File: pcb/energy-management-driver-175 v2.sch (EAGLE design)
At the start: 57 parts, among them T1 BT138-V, T2 BT138-V, T3 BT138-V, T4 BT138-V, T5 BT138-V, T6 BT138-V, T7 BT138-V, T8 BT138-V

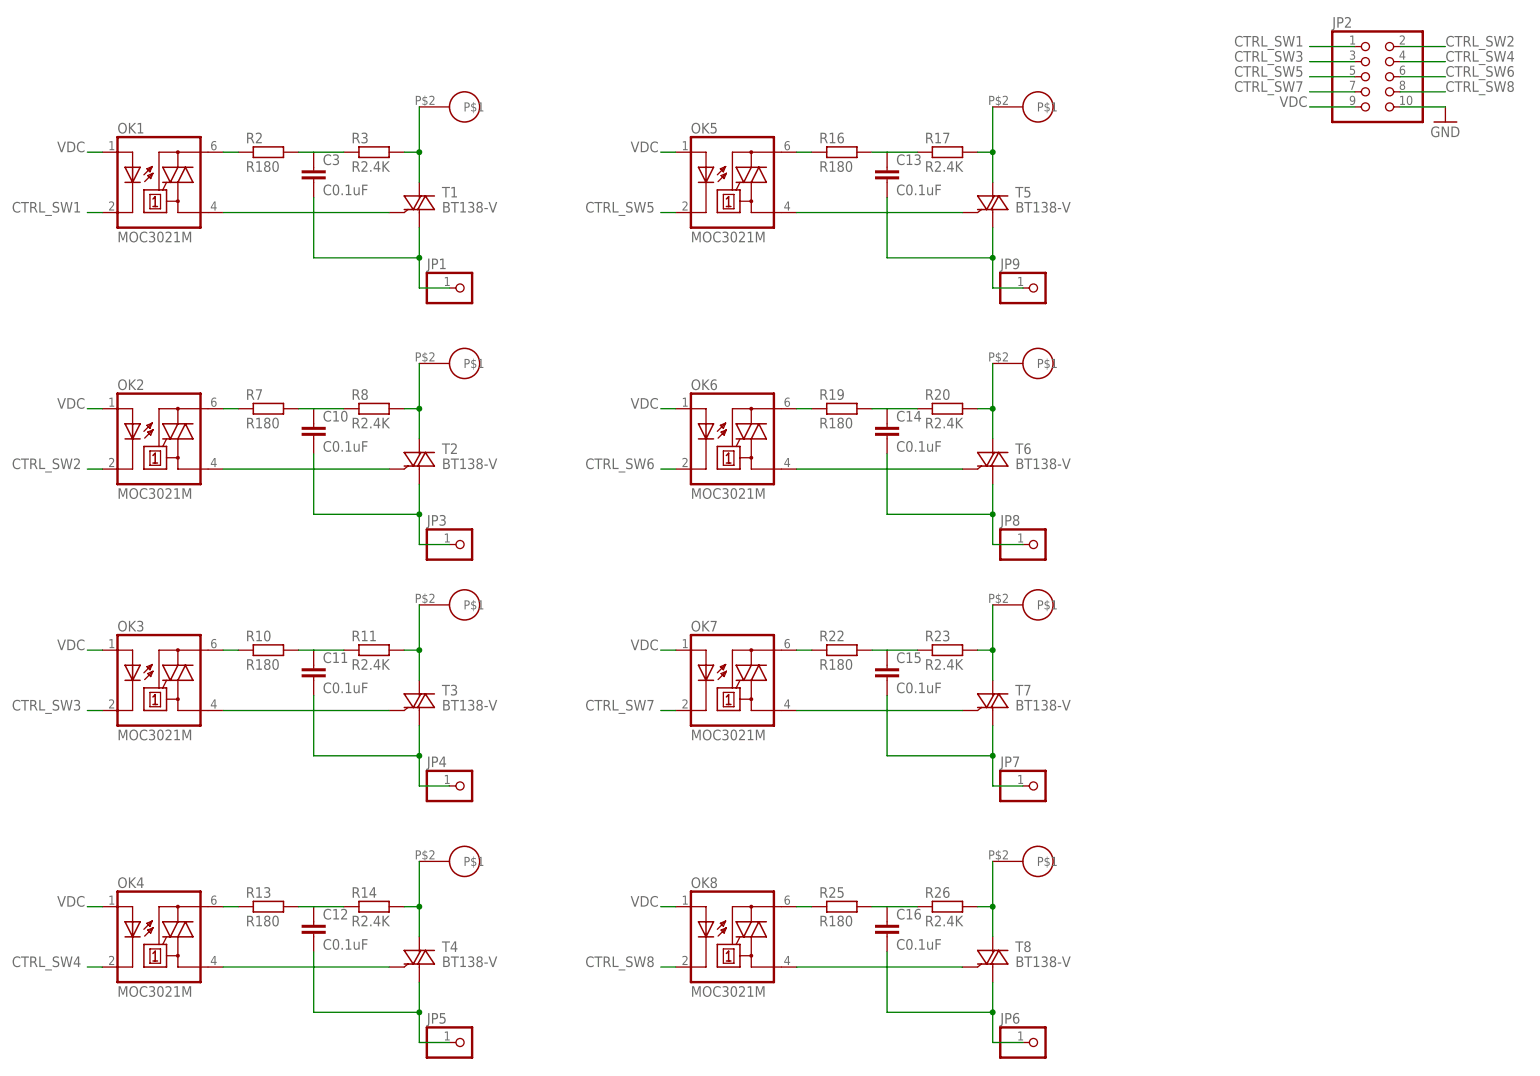
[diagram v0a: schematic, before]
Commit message: update holes in driver board
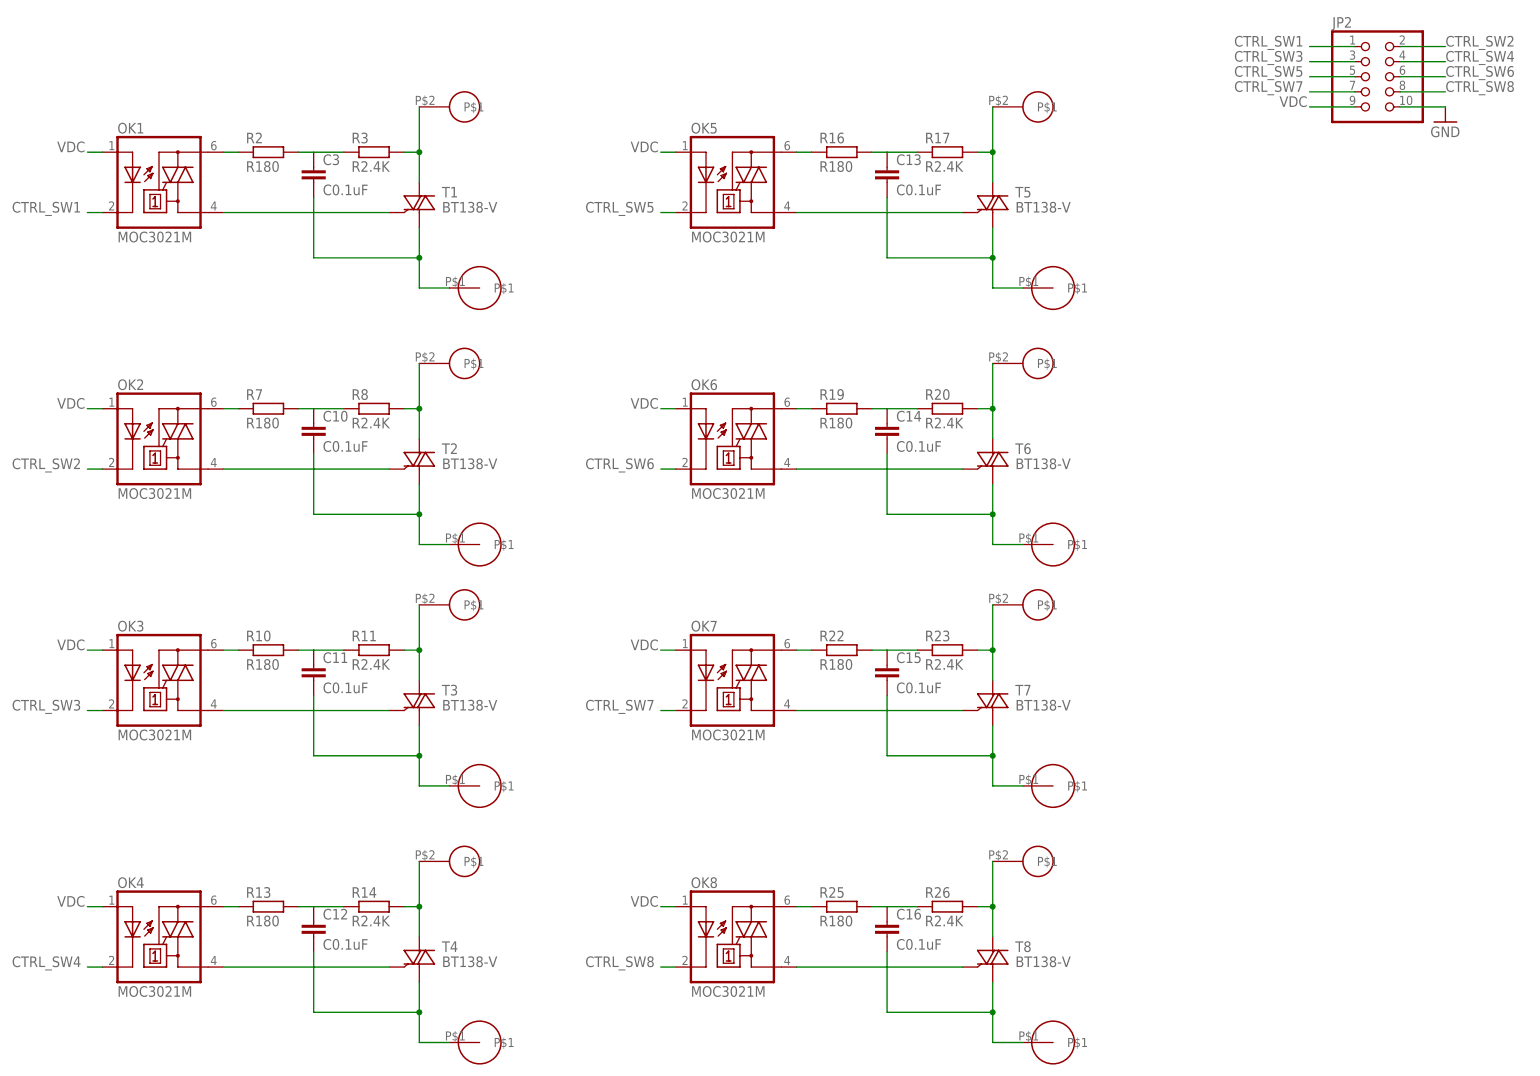
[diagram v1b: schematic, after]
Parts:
- removed JP1, JP3, JP4, JP5, JP6, JP7, JP8, JP9: (no value), pinhead:PINHD-1X1
- added U$10, U$11, U$12, U$13, U$14, U$15, U$16, U$9: CONN-CABLE, bontor:CONN-CABLE
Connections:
- net N$15: now also U$11.P$1; no longer JP3.1
- net N$21: now also U$14.P$1; no longer JP4.1
- net N$27: now also U$13.P$1; no longer JP5.1
- net N$33: now also U$10.P$1; no longer JP9.1
- net N$39: now also U$12.P$1; no longer JP8.1
- net N$45: now also U$15.P$1; no longer JP7.1
- net N$51: now also U$16.P$1; no longer JP6.1
- net N$6: now also U$9.P$1; no longer JP1.1
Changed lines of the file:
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@@
 <part name="JP2" library="pinhead" deviceset="PINHD-2X5" device=""/>
 <part name="GND2" library="SparkFun-Aesthetics" deviceset="GND" device=""/>
-<part name="JP1" library="pinhead" deviceset="PINHD-1X1" device=""/>
 <part name="U$1" library="bontor" deviceset="CONN-SKUN" device=""/>
 <part name="U$2" library="bontor" deviceset="CONN-SKUN" device=""/>
@@
 <part name="U$7" library="bontor" deviceset="CONN-SKUN" device=""/>
 <part name="U$8" library="bontor" deviceset="CONN-SKUN" device=""/>
-<part name="JP3" library="pinhead" deviceset="PINHD-1X1" device=""/>
-<part name="JP4" library="pinhead" deviceset="PINHD-1X1" device=""/>
-<part name="JP5" library="pinhead" deviceset="PINHD-1X1" device=""/>
-<part name="JP6" library="pinhead" deviceset="PINHD-1X1" device=""/>
-<part name="JP7" library="pinhead" deviceset="PINHD-1X1" device=""/>
-<part name="JP8" library="pinhead" deviceset="PINHD-1X1" device=""/>
-<part name="JP9" library="pinhead" deviceset="PINHD-1X1" device=""/>
+<part name="U$9" library="bontor" deviceset="CONN-CABLE" device=""/>
+<part name="U$10" library="bontor" deviceset="CONN-CABLE" device=""/>
+<part name="U$11" library="bontor" deviceset="CONN-CABLE" device=""/>
+<part name="U$12" library="bontor" deviceset="CONN-CABLE" device=""/>
+<part name="U$13" library="bontor" deviceset="CONN-CABLE" device=""/>
+<part name="U$14" library="bontor" deviceset="CONN-CABLE" device=""/>
+<part name="U$15" library="bontor" deviceset="CONN-CABLE" device=""/>
+<part name="U$16" library="bontor" deviceset="CONN-CABLE" device=""/>
 </parts>
 <sheets>
@@
 <instance part="JP2" gate="A" x="241.3" y="172.72"/>
 <instance part="GND2" gate="1" x="254" y="165.1"/>
-<instance part="JP1" gate="G$1" x="88.9" y="137.16"/>
 <instance part="U$1" gate="G$1" x="88.9" y="167.64"/>
 <instance part="U$2" gate="G$1" x="88.9" y="124.46"/>
@@
 <instance part="U$7" gate="G$1" x="185.42" y="124.46"/>
 <instance part="U$8" gate="G$1" x="185.42" y="167.64"/>
-<instance part="JP3" gate="G$1" x="88.9" y="93.98"/>
-<instance part="JP4" gate="G$1" x="88.9" y="53.34"/>
-<instance part="JP5" gate="G$1" x="88.9" y="10.16"/>
-<instance part="JP6" gate="G$1" x="185.42" y="10.16"/>
-<instance part="JP7" gate="G$1" x="185.42" y="53.34"/>
-<instance part="JP8" gate="G$1" x="185.42" y="93.98"/>
-<instance part="JP9" gate="G$1" x="185.42" y="137.16"/>
+<instance part="U$9" gate="G$1" x="91.44" y="137.16"/>
+<instance part="U$10" gate="G$1" x="187.96" y="137.16"/>
+<instance part="U$11" gate="G$1" x="91.44" y="93.98"/>
+<instance part="U$12" gate="G$1" x="187.96" y="93.98"/>
+<instance part="U$13" gate="G$1" x="91.44" y="10.16"/>
+<instance part="U$14" gate="G$1" x="91.44" y="53.34"/>
+<instance part="U$15" gate="G$1" x="187.96" y="53.34"/>
+<instance part="U$16" gate="G$1" x="187.96" y="10.16"/>
 </instances>
 <busses>
@@
 <wire x1="81.28" y1="137.16" x2="81.28" y2="142.24" width="0.1524" layer="91"/>
 <junction x="81.28" y="142.24"/>
-<pinref part="JP1" gate="G$1" pin="1"/>
 <wire x1="86.36" y1="137.16" x2="81.28" y2="137.16" width="0.1524" layer="91"/>
+<pinref part="U$9" gate="G$1" pin="P$1"/>
 </segment>
 </net>
@@
 <wire x1="81.28" y1="93.98" x2="81.28" y2="99.06" width="0.1524" layer="91"/>
 <junction x="81.28" y="99.06"/>
-<pinref part="JP3" gate="G$1" pin="1"/>
 <wire x1="86.36" y1="93.98" x2="81.28" y2="93.98" width="0.1524" layer="91"/>
+<pinref part="U$11" gate="G$1" pin="P$1"/>
 </segment>
 </net>
@@
 <wire x1="81.28" y1="53.34" x2="81.28" y2="58.42" width="0.1524" layer="91"/>
 <junction x="81.28" y="58.42"/>
-<pinref part="JP4" gate="G$1" pin="1"/>
 <wire x1="86.36" y1="53.34" x2="81.28" y2="53.34" width="0.1524" layer="91"/>
+<pinref part="U$14" gate="G$1" pin="P$1"/>
 </segment>
 </net>
@@
 <wire x1="81.28" y1="10.16" x2="81.28" y2="15.24" width="0.1524" layer="91"/>
 <junction x="81.28" y="15.24"/>
-<pinref part="JP5" gate="G$1" pin="1"/>
 <wire x1="86.36" y1="10.16" x2="81.28" y2="10.16" width="0.1524" layer="91"/>
+<pinref part="U$13" gate="G$1" pin="P$1"/>
 </segment>
 </net>
@@
 <wire x1="177.8" y1="137.16" x2="177.8" y2="142.24" width="0.1524" layer="91"/>
 <junction x="177.8" y="142.24"/>
-<pinref part="JP9" gate="G$1" pin="1"/>
 <wire x1="182.88" y1="137.16" x2="177.8" y2="137.16" width="0.1524" layer="91"/>
+<pinref part="U$10" gate="G$1" pin="P$1"/>
 </segment>
 </net>
@@
 <wire x1="177.8" y1="99.06" x2="177.8" y2="93.98" width="0.1524" layer="91"/>
 <junction x="177.8" y="99.06"/>
-<pinref part="JP8" gate="G$1" pin="1"/>
 <wire x1="182.88" y1="93.98" x2="177.8" y2="93.98" width="0.1524" layer="91"/>
+<pinref part="U$12" gate="G$1" pin="P$1"/>
 </segment>
 </net>
@@
 <wire x1="177.8" y1="58.42" x2="177.8" y2="53.34" width="0.1524" layer="91"/>
 <junction x="177.8" y="58.42"/>
-<pinref part="JP7" gate="G$1" pin="1"/>
 <wire x1="182.88" y1="53.34" x2="177.8" y2="53.34" width="0.1524" layer="91"/>
+<pinref part="U$15" gate="G$1" pin="P$1"/>
 </segment>
 </net>
@@
 <wire x1="177.8" y1="15.24" x2="177.8" y2="10.16" width="0.1524" layer="91"/>
 <junction x="177.8" y="15.24"/>
-<pinref part="JP6" gate="G$1" pin="1"/>
 <wire x1="182.88" y1="10.16" x2="177.8" y2="10.16" width="0.1524" layer="91"/>
-</segment>
-</net>
+<pinref part="U$16" gate="G$1" pin="P$1"/>
+</segment>
+</net>
